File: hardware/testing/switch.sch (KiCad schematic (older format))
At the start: 32 parts

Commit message: starting the testing PCB
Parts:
- added CherryMX10, CherryMX15, CherryMX20, CherryMX21, CherryMX22, CherryMX23, CherryMX24, CherryMX25, CherryMX26, CherryMX27, CherryMX28, CherryMX29, CherryMX30, CherryMX31, CherryMX32, CherryMX33, CherryMX34, CherryMX35, CherryMX36, CherryMX37, CherryMX38, CherryMX39, CherryMX40, CherryMX41, CherryMX42, CherryMX43, CherryMX44, CherryMX45, CherryMX46, CherryMX47, CherryMX48, CherryMX49, CherryMX5, CherryMX50, CherryMX51, CherryMX52, CherryMX53, CherryMX54, CherryMX55, CherryMX56, CherryMX57, CherryMX58, CherryMX59, CherryMX60, CherryMX61, CherryMX62, CherryMX63, CherryMX64, CherryMX65, CherryMX66, CherryMX67, CherryMX68: SW_SPST, TestPoint:TestPoint_2Pads_Pitch2.54mm_Drill0.8mm, symbol Switch:SW_SPST
- added D10, D15, D20, D21, D22, D23, D24, D25, D26, D27, D28, D29, D30, D31, D32, D33, D34, D35, D36, D37, D38, D39, D40, D41, D42, D43, D44, D45, D46, D47, D48, D49, D5, D50, D51, D52, D53, D54, D55, D56, D57, D58, D59, D60, D61, D62, D63, D64, D65, D66, D67, D68: 1N4148W, Diode_SMD:D_SOD-523, symbol Diode:1N4148W
- CherryMX1, CherryMX2, CherryMX3, CherryMX4: footprint Button_Switch_Keyboard:SW_Cherry_MX_1.00u_Plate -> TestPoint:TestPoint_2Pads_Pitch2.54mm_Drill0.8mm; Footprint (none) -> keyswitches:Kailh_socket_MX_optional_reversible
- CherryMX11: renamed from CherryMX9; footprint Button_Switch_Keyboard:SW_Cherry_MX_1.00u_Plate -> TestPoint:TestPoint_2Pads_Pitch2.54mm_Drill0.8mm; Footprint (none) -> keyswitches:Kailh_socket_MX_optional_reversible
- CherryMX12: renamed from CherryMX10; footprint Button_Switch_Keyboard:SW_Cherry_MX_1.00u_Plate -> TestPoint:TestPoint_2Pads_Pitch2.54mm_Drill0.8mm; Footprint (none) -> keyswitches:Kailh_socket_MX_optional_reversible
- CherryMX13: renamed from CherryMX11; footprint Button_Switch_Keyboard:SW_Cherry_MX_1.00u_Plate -> TestPoint:TestPoint_2Pads_Pitch2.54mm_Drill0.8mm; Footprint (none) -> keyswitches:Kailh_socket_MX_optional_reversible
- CherryMX14: renamed from CherryMX12; footprint Button_Switch_Keyboard:SW_Cherry_MX_1.00u_Plate -> TestPoint:TestPoint_2Pads_Pitch2.54mm_Drill0.8mm; Footprint (none) -> keyswitches:Kailh_socket_MX_optional_reversible
- CherryMX16: renamed from CherryMX13; footprint Button_Switch_Keyboard:SW_Cherry_MX_1.00u_Plate -> TestPoint:TestPoint_2Pads_Pitch2.54mm_Drill0.8mm; Footprint (none) -> keyswitches:Kailh_socket_MX_optional_reversible
- CherryMX17: renamed from CherryMX14; footprint Button_Switch_Keyboard:SW_Cherry_MX_1.00u_Plate -> TestPoint:TestPoint_2Pads_Pitch2.54mm_Drill0.8mm; Footprint (none) -> keyswitches:Kailh_socket_MX_optional_reversible
- CherryMX18: renamed from CherryMX15; footprint Button_Switch_Keyboard:SW_Cherry_MX_1.00u_Plate -> TestPoint:TestPoint_2Pads_Pitch2.54mm_Drill0.8mm; Footprint (none) -> keyswitches:Kailh_socket_MX_optional_reversible
- CherryMX19: renamed from CherryMX16; footprint Button_Switch_Keyboard:SW_Cherry_MX_1.00u_Plate -> TestPoint:TestPoint_2Pads_Pitch2.54mm_Drill0.8mm; Footprint (none) -> keyswitches:Kailh_socket_MX_optional_reversible
- CherryMX6: renamed from CherryMX5; footprint Button_Switch_Keyboard:SW_Cherry_MX_1.00u_Plate -> TestPoint:TestPoint_2Pads_Pitch2.54mm_Drill0.8mm; Footprint (none) -> keyswitches:Kailh_socket_MX_optional_reversible
- CherryMX7: renamed from CherryMX6; footprint Button_Switch_Keyboard:SW_Cherry_MX_1.00u_Plate -> TestPoint:TestPoint_2Pads_Pitch2.54mm_Drill0.8mm; Footprint (none) -> keyswitches:Kailh_socket_MX_optional_reversible
- CherryMX8: renamed from CherryMX7; footprint Button_Switch_Keyboard:SW_Cherry_MX_1.00u_Plate -> TestPoint:TestPoint_2Pads_Pitch2.54mm_Drill0.8mm; Footprint (none) -> keyswitches:Kailh_socket_MX_optional_reversible
- CherryMX9: renamed from CherryMX8; footprint Button_Switch_Keyboard:SW_Cherry_MX_1.00u_Plate -> TestPoint:TestPoint_2Pads_Pitch2.54mm_Drill0.8mm; Footprint (none) -> keyswitches:Kailh_socket_MX_optional_reversible
- D1, D2, D3, D4: footprint Diode_SMD:D_SOD-123 -> Diode_SMD:D_SOD-523; Footprint (none) -> Diode_SMD:D_SOD-123
- D11: renamed from D9; footprint Diode_SMD:D_SOD-123 -> Diode_SMD:D_SOD-523; Footprint (none) -> Diode_SMD:D_SOD-123
- D12: renamed from D10; footprint Diode_SMD:D_SOD-123 -> Diode_SMD:D_SOD-523; Footprint (none) -> Diode_SMD:D_SOD-123
- D13: renamed from D11; footprint Diode_SMD:D_SOD-123 -> Diode_SMD:D_SOD-523; Footprint (none) -> Diode_SMD:D_SOD-123
- D14: renamed from D12; footprint Diode_SMD:D_SOD-123 -> Diode_SMD:D_SOD-523; Footprint (none) -> Diode_SMD:D_SOD-123
- D16: renamed from D13; footprint Diode_SMD:D_SOD-123 -> Diode_SMD:D_SOD-523; Footprint (none) -> Diode_SMD:D_SOD-123
- D17: renamed from D14; footprint Diode_SMD:D_SOD-123 -> Diode_SMD:D_SOD-523; Footprint (none) -> Diode_SMD:D_SOD-123
- D18: renamed from D15; footprint Diode_SMD:D_SOD-123 -> Diode_SMD:D_SOD-523; Footprint (none) -> Diode_SMD:D_SOD-123
- D19: renamed from D16; footprint Diode_SMD:D_SOD-123 -> Diode_SMD:D_SOD-523; Footprint (none) -> Diode_SMD:D_SOD-123
- D6: renamed from D5; footprint Diode_SMD:D_SOD-123 -> Diode_SMD:D_SOD-523; Footprint (none) -> Diode_SMD:D_SOD-123
- D7: renamed from D6; footprint Diode_SMD:D_SOD-123 -> Diode_SMD:D_SOD-523; Footprint (none) -> Diode_SMD:D_SOD-123
- D8: renamed from D7; footprint Diode_SMD:D_SOD-123 -> Diode_SMD:D_SOD-523; Footprint (none) -> Diode_SMD:D_SOD-123
- D9: renamed from D8; footprint Diode_SMD:D_SOD-123 -> Diode_SMD:D_SOD-523; Footprint (none) -> Diode_SMD:D_SOD-123
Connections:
- net COL1: now also D65.1 (K), D66.1 (K), D67.1 (K), D68.1 (K); no longer D1.1 (K), D2.1 (K), D3.1 (K), D4.1 (K)
- net COL2: now also D60.1 (K), D61.1 (K), D62.1 (K), D63.1 (K), D64.1 (K); no longer D6.1 (K), D7.1 (K), D8.1 (K), D9.1 (K)
- net COL3: now also D55.1 (K), D56.1 (K), D57.1 (K), D58.1 (K), D59.1 (K); no longer D11.1 (K), D12.1 (K), D13.1 (K), D14.1 (K)
- net COL4: now also D50.1 (K), D51.1 (K), D52.1 (K), D53.1 (K), D54.1 (K); no longer D16.1 (K), D17.1 (K), D18.1 (K), D19.1 (K)
- net ROW1: now also CherryMX21.1 (A), CherryMX26.1 (A), CherryMX31.1 (A), CherryMX35.1 (A), CherryMX40.1 (A), CherryMX45.1 (A), CherryMX50.1 (A), CherryMX55.1 (A), CherryMX60.1 (A), CherryMX65.1 (A)
- net ROW2: now also CherryMX22.1 (A), CherryMX27.1 (A), CherryMX32.1 (A), CherryMX36.1 (A), CherryMX41.1 (A), CherryMX46.1 (A), CherryMX51.1 (A), CherryMX56.1 (A), CherryMX61.1 (A), CherryMX66.1 (A)
- net ROW3: now also CherryMX23.1 (A), CherryMX28.1 (A), CherryMX33.1 (A), CherryMX37.1 (A), CherryMX42.1 (A), CherryMX47.1 (A), CherryMX52.1 (A), CherryMX57.1 (A), CherryMX62.1 (A)
- net ROW4: now also CherryMX24.1 (A), CherryMX29.1 (A), CherryMX34.1 (A), CherryMX38.1 (A), CherryMX43.1 (A), CherryMX48.1 (A), CherryMX53.1 (A), CherryMX58.1 (A), CherryMX63.1 (A), CherryMX67.1 (A)
- new net: CherryMX5.2 (B), D5.2 (A)
- new net: CherryMX10.2 (B), D10.2 (A)
- new net: CherryMX15.2 (B), D15.2 (A)
- new net: CherryMX20.2 (B), D20.2 (A)
- new net: CherryMX21.2 (B), D21.2 (A)
- new net: CherryMX22.2 (B), D22.2 (A)
- new net: CherryMX23.2 (B), D23.2 (A)
- new net: CherryMX24.2 (B), D24.2 (A)
- new net: CherryMX25.2 (B), D25.2 (A)
- new net: CherryMX26.2 (B), D26.2 (A)
- new net: CherryMX27.2 (B), D27.2 (A)
- new net: CherryMX28.2 (B), D28.2 (A)
- new net: CherryMX29.2 (B), D29.2 (A)
- new net: CherryMX30.2 (B), D30.2 (A)
- new net: CherryMX31.2 (B), D31.2 (A)
- new net: CherryMX32.2 (B), D32.2 (A)
- new net: CherryMX33.2 (B), D33.2 (A)
- new net: CherryMX34.2 (B), D34.2 (A)
- new net: CherryMX35.2 (B), D35.2 (A)
- new net: CherryMX36.2 (B), D36.2 (A)
- new net: CherryMX37.2 (B), D37.2 (A)
- new net: CherryMX38.2 (B), D38.2 (A)
- new net: CherryMX39.2 (B), D39.2 (A)
- new net: CherryMX40.2 (B), D40.2 (A)
- new net: CherryMX41.2 (B), D41.2 (A)
- new net: CherryMX42.2 (B), D42.2 (A)
- new net: CherryMX43.2 (B), D43.2 (A)
- new net: CherryMX44.2 (B), D44.2 (A)
- new net: CherryMX45.2 (B), D45.2 (A)
- new net: CherryMX46.2 (B), D46.2 (A)
- new net: CherryMX47.2 (B), D47.2 (A)
- new net: CherryMX48.2 (B), D48.2 (A)
- new net: CherryMX49.2 (B), D49.2 (A)
- new net: CherryMX50.2 (B), D50.2 (A)
- new net: CherryMX51.2 (B), D51.2 (A)
- new net: CherryMX52.2 (B), D52.2 (A)
- new net: CherryMX53.2 (B), D53.2 (A)
- new net: CherryMX54.2 (B), D54.2 (A)
- new net: CherryMX55.2 (B), D55.2 (A)
- new net: CherryMX56.2 (B), D56.2 (A)
- new net: CherryMX57.2 (B), D57.2 (A)
- new net: CherryMX58.2 (B), D58.2 (A)
- new net: CherryMX59.2 (B), D59.2 (A)
- new net: CherryMX60.2 (B), D60.2 (A)
- new net: CherryMX61.2 (B), D61.2 (A)
- new net: CherryMX62.2 (B), D62.2 (A)
- new net: CherryMX63.2 (B), D63.2 (A)
- new net: CherryMX64.2 (B), D64.2 (A)
- new net: CherryMX65.2 (B), D65.2 (A)
- new net: CherryMX66.2 (B), D66.2 (A)
- new net: CherryMX67.2 (B), D67.2 (A)
- new net: CherryMX68.2 (B), D68.2 (A)
- new net COL10: D21.1 (K), D22.1 (K), D23.1 (K), D24.1 (K), D25.1 (K)
- new net COL11: D16.1 (K), D17.1 (K), D18.1 (K), D19.1 (K), D20.1 (K)
- new net COL12: D11.1 (K), D12.1 (K), D13.1 (K), D14.1 (K), D15.1 (K)
- new net COL13: D10.1 (K), D6.1 (K), D7.1 (K), D8.1 (K), D9.1 (K)
- new net COL14: D1.1 (K), D2.1 (K), D3.1 (K), D4.1 (K), D5.1 (K)
- new net COL5: D45.1 (K), D46.1 (K), D47.1 (K), D48.1 (K), D49.1 (K)
- new net COL6: D40.1 (K), D41.1 (K), D42.1 (K), D43.1 (K), D44.1 (K)
- new net COL7: D35.1 (K), D36.1 (K), D37.1 (K), D38.1 (K), D39.1 (K)
- new net COL8: D31.1 (K), D32.1 (K), D33.1 (K), D34.1 (K)
- new net COL9: D26.1 (K), D27.1 (K), D28.1 (K), D29.1 (K), D30.1 (K)
- new net ROW5: CherryMX10.1 (A), CherryMX15.1 (A), CherryMX20.1 (A), CherryMX25.1 (A), CherryMX30.1 (A), CherryMX39.1 (A), CherryMX44.1 (A), CherryMX49.1 (A), CherryMX5.1 (A), CherryMX54.1 (A), CherryMX59.1 (A), CherryMX64.1 (A), CherryMX68.1 (A)

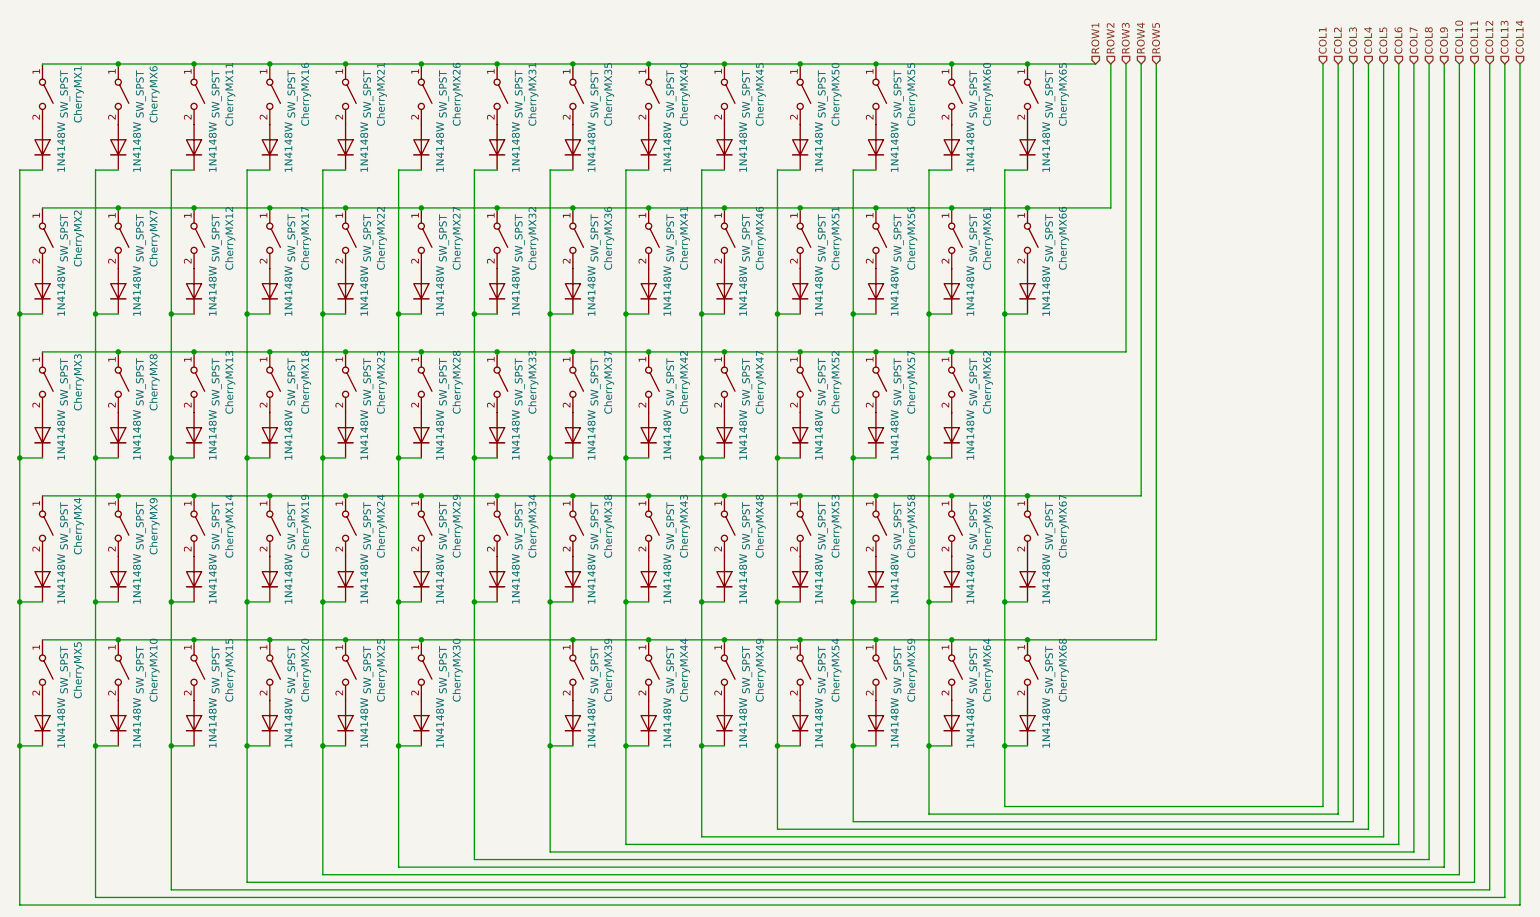
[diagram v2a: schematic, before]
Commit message: making testing PCB, making sure the DFU mode is correct
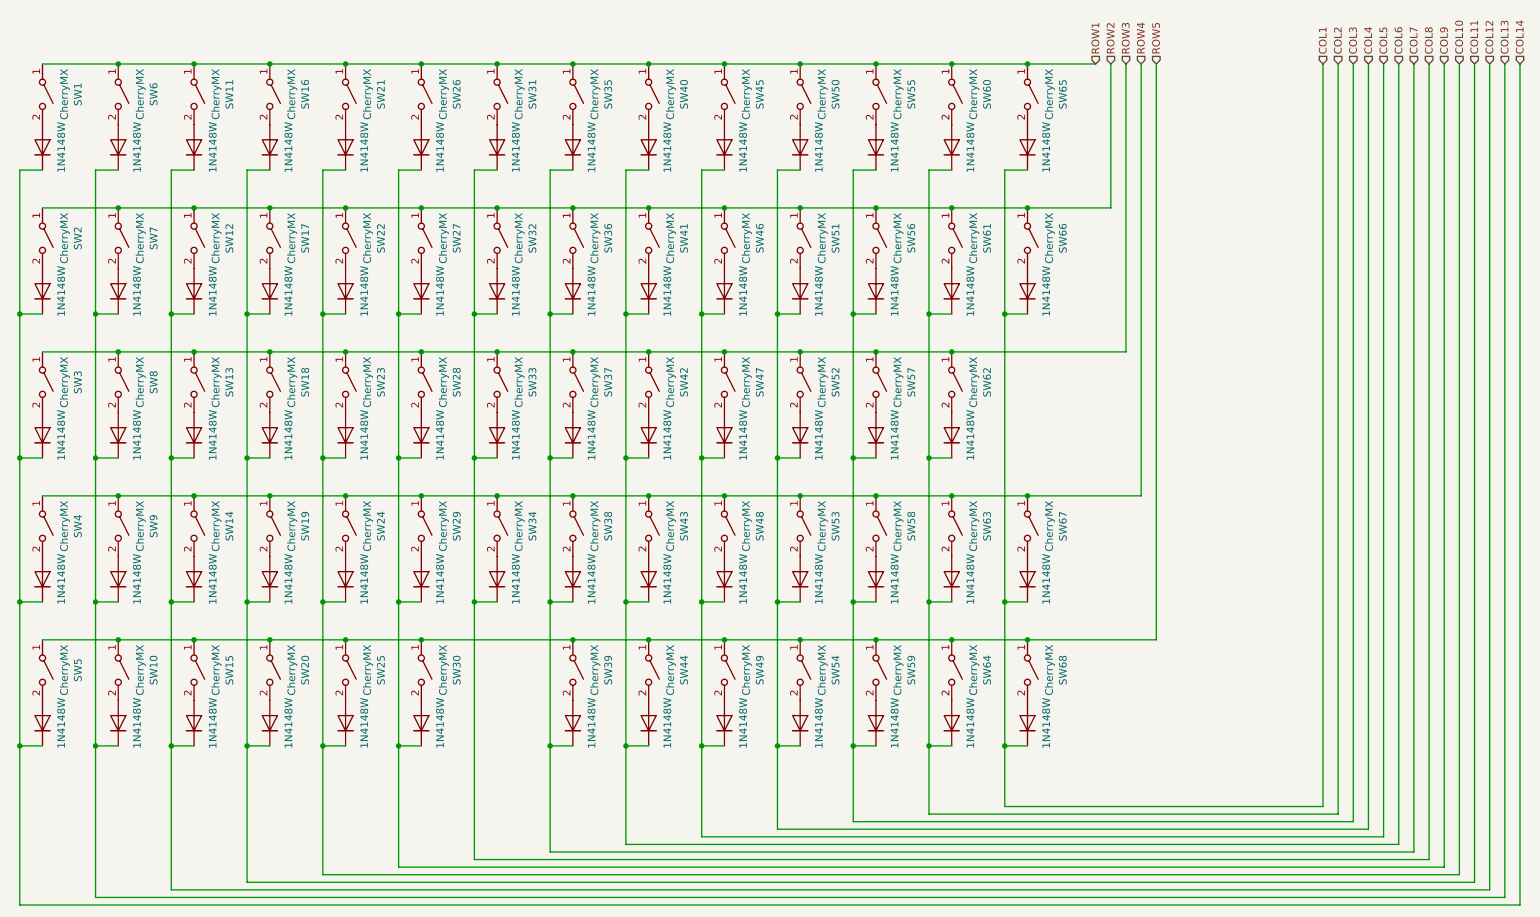
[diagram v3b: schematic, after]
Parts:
- SW1: renamed from CherryMX1; value SW_SPST -> CherryMX
- SW10: renamed from CherryMX10; value SW_SPST -> CherryMX
- SW11: renamed from CherryMX11; value SW_SPST -> CherryMX
- SW12: renamed from CherryMX12; value SW_SPST -> CherryMX
- SW13: renamed from CherryMX13; value SW_SPST -> CherryMX
- SW14: renamed from CherryMX14; value SW_SPST -> CherryMX
- SW15: renamed from CherryMX15; value SW_SPST -> CherryMX
- SW16: renamed from CherryMX16; value SW_SPST -> CherryMX
- SW17: renamed from CherryMX17; value SW_SPST -> CherryMX
- SW18: renamed from CherryMX18; value SW_SPST -> CherryMX
- SW19: renamed from CherryMX19; value SW_SPST -> CherryMX
- SW2: renamed from CherryMX2; value SW_SPST -> CherryMX
- SW20: renamed from CherryMX20; value SW_SPST -> CherryMX
- SW21: renamed from CherryMX21; value SW_SPST -> CherryMX
- SW22: renamed from CherryMX22; value SW_SPST -> CherryMX
- SW23: renamed from CherryMX23; value SW_SPST -> CherryMX
- SW24: renamed from CherryMX24; value SW_SPST -> CherryMX
- SW25: renamed from CherryMX25; value SW_SPST -> CherryMX
- SW26: renamed from CherryMX26; value SW_SPST -> CherryMX
- SW27: renamed from CherryMX27; value SW_SPST -> CherryMX
- SW28: renamed from CherryMX28; value SW_SPST -> CherryMX
- SW29: renamed from CherryMX29; value SW_SPST -> CherryMX
- SW3: renamed from CherryMX3; value SW_SPST -> CherryMX
- SW30: renamed from CherryMX30; value SW_SPST -> CherryMX
- SW31: renamed from CherryMX31; value SW_SPST -> CherryMX
- SW32: renamed from CherryMX32; value SW_SPST -> CherryMX
- SW33: renamed from CherryMX33; value SW_SPST -> CherryMX
- SW34: renamed from CherryMX34; value SW_SPST -> CherryMX
- SW35: renamed from CherryMX35; value SW_SPST -> CherryMX
- SW36: renamed from CherryMX36; value SW_SPST -> CherryMX
- SW37: renamed from CherryMX37; value SW_SPST -> CherryMX
- SW38: renamed from CherryMX38; value SW_SPST -> CherryMX
- SW39: renamed from CherryMX39; value SW_SPST -> CherryMX
- SW4: renamed from CherryMX4; value SW_SPST -> CherryMX
- SW40: renamed from CherryMX40; value SW_SPST -> CherryMX
- SW41: renamed from CherryMX41; value SW_SPST -> CherryMX
- SW42: renamed from CherryMX42; value SW_SPST -> CherryMX
- SW43: renamed from CherryMX43; value SW_SPST -> CherryMX
- SW44: renamed from CherryMX44; value SW_SPST -> CherryMX
- SW45: renamed from CherryMX45; value SW_SPST -> CherryMX
- SW46: renamed from CherryMX46; value SW_SPST -> CherryMX
- SW47: renamed from CherryMX47; value SW_SPST -> CherryMX
- SW48: renamed from CherryMX48; value SW_SPST -> CherryMX
- SW49: renamed from CherryMX49; value SW_SPST -> CherryMX
- SW5: renamed from CherryMX5; value SW_SPST -> CherryMX
- SW50: renamed from CherryMX50; value SW_SPST -> CherryMX
- SW51: renamed from CherryMX51; value SW_SPST -> CherryMX
- SW52: renamed from CherryMX52; value SW_SPST -> CherryMX
- SW53: renamed from CherryMX53; value SW_SPST -> CherryMX
- SW54: renamed from CherryMX54; value SW_SPST -> CherryMX
- SW55: renamed from CherryMX55; value SW_SPST -> CherryMX
- SW56: renamed from CherryMX56; value SW_SPST -> CherryMX
- SW57: renamed from CherryMX57; value SW_SPST -> CherryMX
- SW58: renamed from CherryMX58; value SW_SPST -> CherryMX
- SW59: renamed from CherryMX59; value SW_SPST -> CherryMX
- SW6: renamed from CherryMX6; value SW_SPST -> CherryMX
- SW60: renamed from CherryMX60; value SW_SPST -> CherryMX
- SW61: renamed from CherryMX61; value SW_SPST -> CherryMX
- SW62: renamed from CherryMX62; value SW_SPST -> CherryMX
- SW63: renamed from CherryMX63; value SW_SPST -> CherryMX
- SW64: renamed from CherryMX64; value SW_SPST -> CherryMX
- SW65: renamed from CherryMX65; value SW_SPST -> CherryMX
- SW66: renamed from CherryMX66; value SW_SPST -> CherryMX
- SW67: renamed from CherryMX67; value SW_SPST -> CherryMX
- SW68: renamed from CherryMX68; value SW_SPST -> CherryMX
- SW7: renamed from CherryMX7; value SW_SPST -> CherryMX
- SW8: renamed from CherryMX8; value SW_SPST -> CherryMX
- SW9: renamed from CherryMX9; value SW_SPST -> CherryMX

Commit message: Full Send, SMT assembly LOL
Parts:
- D1, D10, D11, D12, D13, D14, D15, D16, D17, D18, D19, D2, D20, D21, D22, D23, D24, D25, D26, D27, D28, D29, D3, D30, D31, D32, D33, D34, D35, D36, D37, D38, D39, D4, D40, D41, D42, D43, D44, D45, D46, D47, D48, D49, D5, D50, D51, D52, D53, D54, D55, D56, D57, D58, D59, D6, D60, D61, D62, D63, D64, D65, D66, D67, D68, D7, D8, D9: value 1N4148W -> 1N4148WT
- SW1, SW10, SW11, SW12, SW13, SW14, SW15, SW16, SW17, SW18, SW19, SW2, SW20, SW21, SW22, SW23, SW24, SW25, SW26, SW27, SW28, SW29, SW3, SW30, SW31, SW32, SW33, SW34, SW35, SW36, SW37, SW38, SW39, SW4, SW40, SW41, SW42, SW43, SW44, SW45, SW46, SW47, SW48, SW49, SW5, SW50, SW51, SW52, SW53, SW54, SW55, SW56, SW57, SW58, SW59, SW6, SW60, SW61, SW62, SW63, SW64, SW65, SW66, SW67, SW68, SW7, SW8, SW9: value CherryMX -> SW
